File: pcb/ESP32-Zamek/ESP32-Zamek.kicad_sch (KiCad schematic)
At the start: 14 parts, among them J1 Conn_01x02_Socket, J4 Conn_01x02_Socket, Q3 SQ4940CEY-T1_GE3, SW3 CK_KMS2xxG

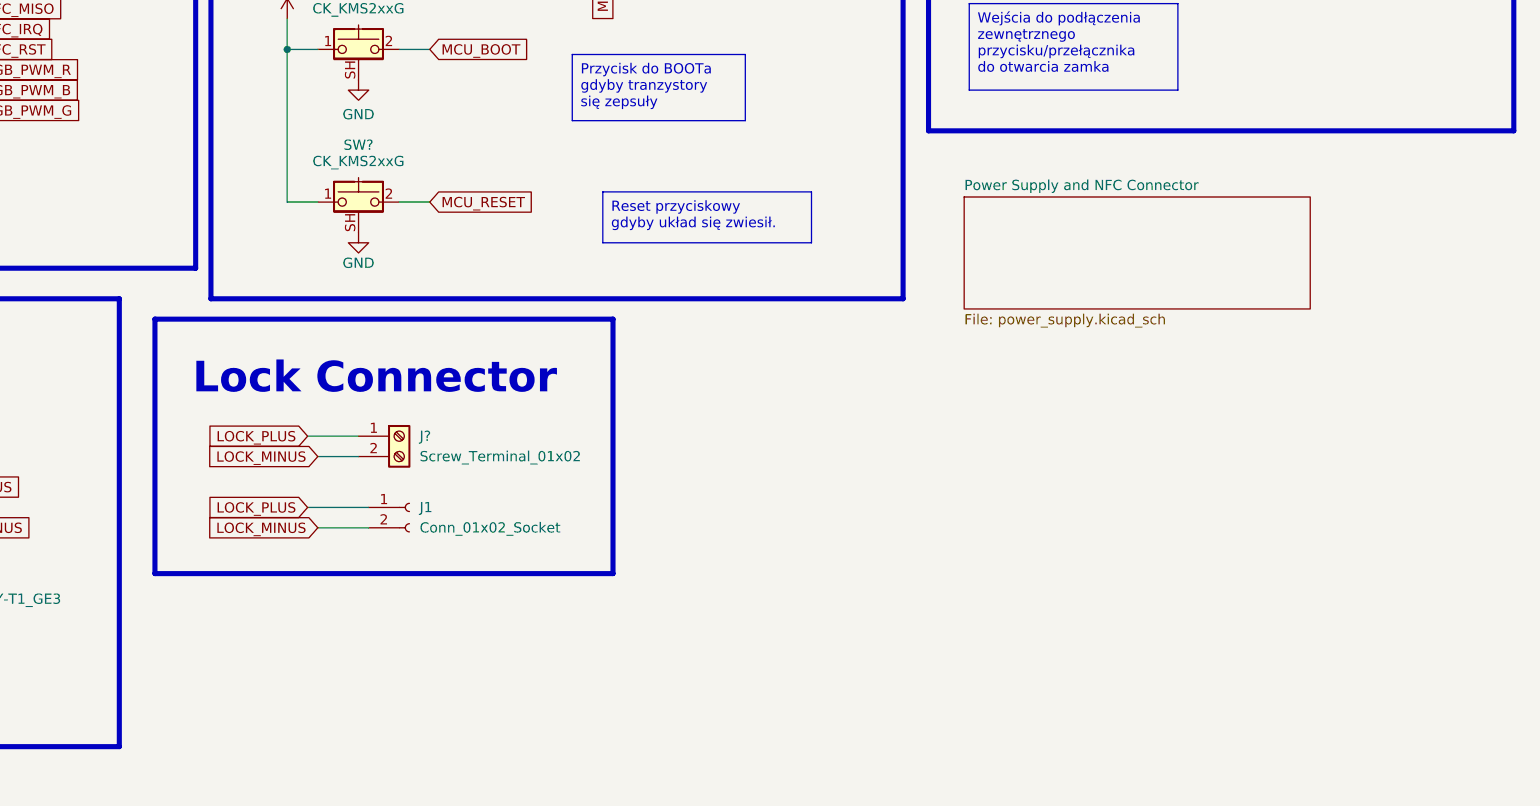
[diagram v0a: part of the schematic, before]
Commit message: Add a buzzer controller to the schematic
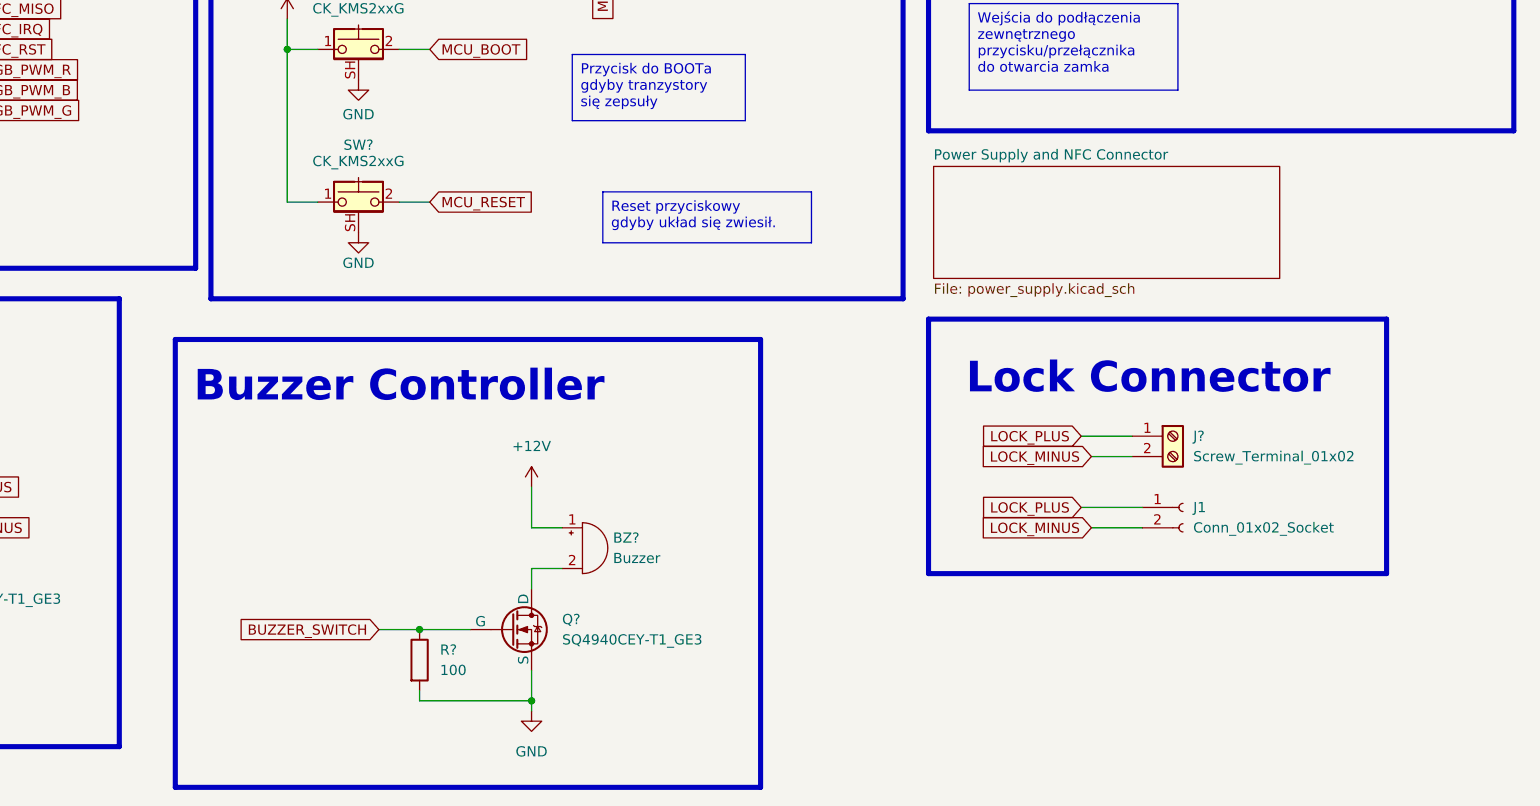
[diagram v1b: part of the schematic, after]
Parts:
- added BZ?: Buzzer, symbol Device:Buzzer
- added Q?: SQ4940CEY-T1_GE3, symbol Simulation_SPICE:NMOS
- added R?: 100, symbol Device:R
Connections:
- net +12V: now also BZ?.1 (+)
- net BUZZER_SWITCH: now also Q?.2 (G), R?.1
- net GND: now also Q?.3 (S), R?.2
- new net: BZ?.2 (-), Q?.1 (D)
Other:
- note added: "Buzzer Controller"
- moved on the sheet: J1, J?

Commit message: Added Connectors, Fixed buttons
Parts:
- removed J1: Conn_01x02_Socket, symbol Connector:Conn_01x02_Socket
- removed J? (x2): Screw_Terminal_01x02, symbol Connector:Screw_Terminal_01x02
- removed SW3, SW? (x2): CK_KMS2xxG, Button_Switch_SMD:SW_SPST_CK_KMS2xxGP, symbol Switch:CK_KMS2xxG
- added C1, C2, C3, C5: 0.1u, symbol Device:C
- added C4: 22u, symbol Device:C
- added D1: LED_ARGB, symbol Device:LED_ARGB
- added SW1, SW2, SW3: SW_Push, symbol Switch:SW_Push
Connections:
- net +3.3V: now also C3.1, C4.1, C5.1, D1.1 (A), SW3.1
- net GND: now also C1.1, C2.1, C3.2, C4.2, SW1.1, SW2.1
- net LOCK_MCU_MANUAL_OPEN: now also C5.2, SW3.2
- net MCU_BOOT: now also C1.2, SW1.2
- net MCU_RESET: now also C2.2, SW2.2
- net FREE_GPIO_1: now reaches U?.24 (IO2)
- net FREE_GPIO_3: now reaches U?.27 (IO16)
- net FREE_GPIO_4: now reaches U?.28 (IO17)
- net FREE_GPIO_7: now reaches U?.7 (IO35)
- net NFC_EEPROM_SCL: no longer names the net of U?.36 (IO22)
- net NFC_EEPROM_SDA: no longer names the net of U?.33 (IO21)
- net RGB_PWM_B: no longer names the net of U?.9 (IO33)
- net RGB_PWM_B: now also D1.3 (GK)
- net RGB_PWM_G: no longer names the net of U?.6 (IO34)
- net RGB_PWM_G: now also D1.4 (BK)
- net RGB_PWM_R: no longer names the net of U?.8 (IO32)
- net RGB_PWM_R: now also D1.2 (RK)
- no-connect marks 12 -> 8
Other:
- added sheet Connnectors (Connectors_sch.kicad_sch)
- note removed: "Do zastanowienia się ten JTAG"
- note removed: "EEPROM"
- note removed: "JTAG"
- note removed: "Lock Connector"
- note removed: "NIE WIEM CO TO"
- note removed: "RGB LED"
- moved on the sheet: J4, Q3, R1, U?

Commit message: Add one note
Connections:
- net FREE_GPIO_2: now also U?.29 (IO5)
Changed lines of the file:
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@@
+	(wire
+		(pts
+			(xy 64.77 60.96) (xy 71.12 60.96)
+		)
+		(stroke
+			(width 0)
+			(type default)
+		)
+	)
 	(wire
 		(pts
